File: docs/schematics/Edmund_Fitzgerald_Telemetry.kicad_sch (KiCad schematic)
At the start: 14 parts, among them Q1 MOSFET_N, Q2 MOSFET_N, U1 ESP32_Control, U2 MAX98357A, U3 DFPlayer_Pro, U4 ESP32-CAM

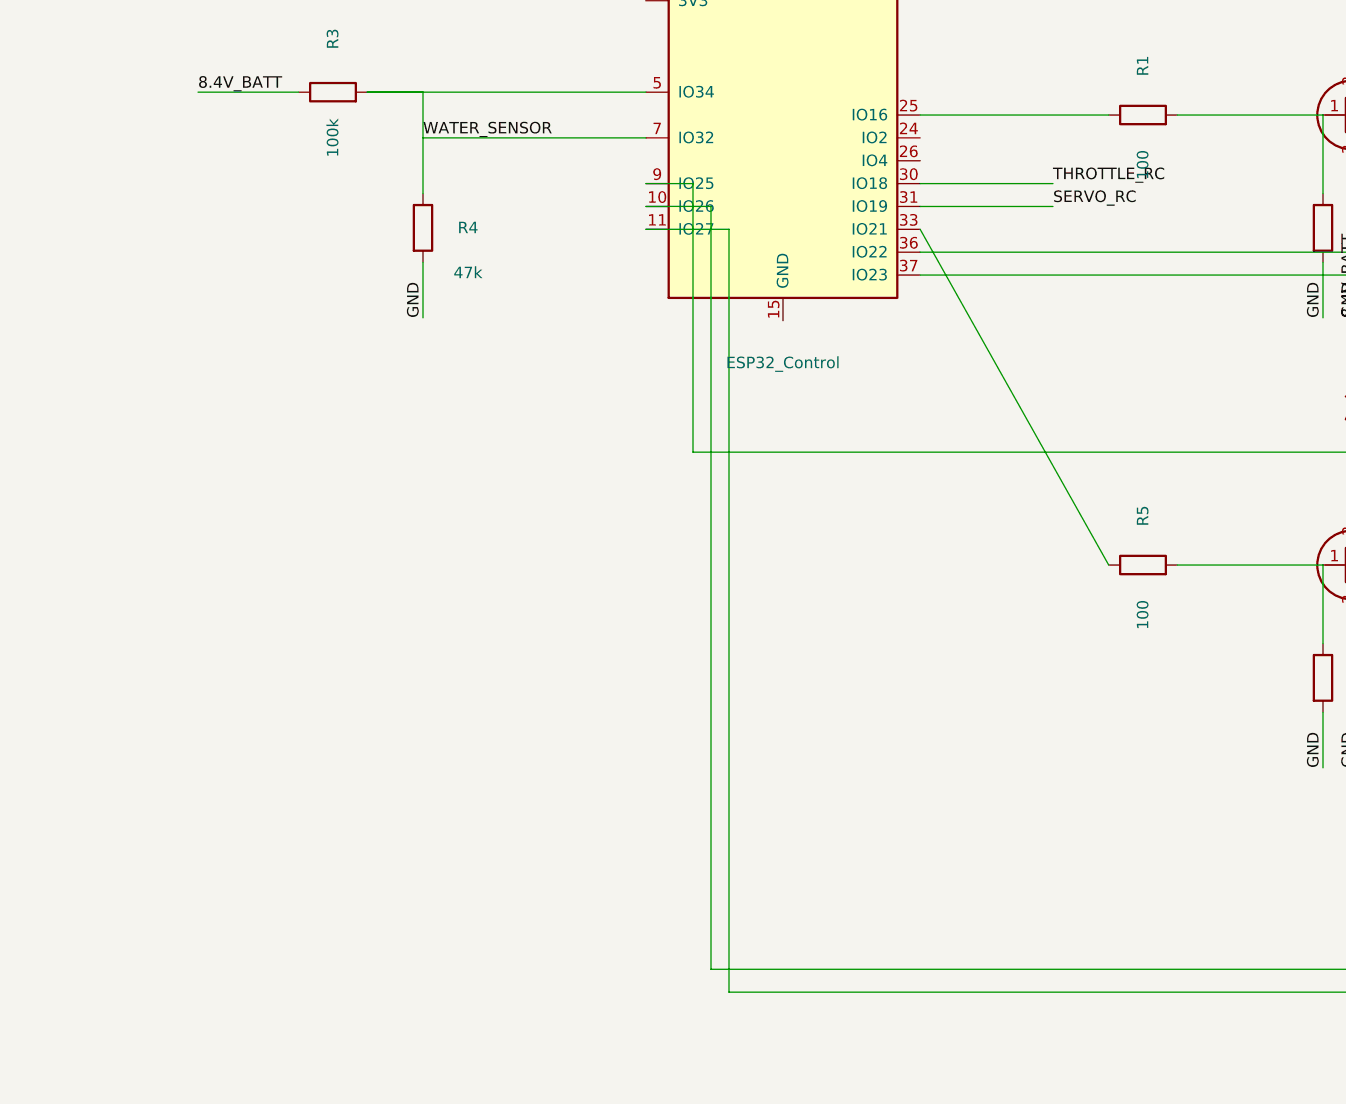
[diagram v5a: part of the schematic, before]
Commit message: Schematic update: Added physical RC and Servo wiring
- Replaced RC labels with physical orthogonal wires
- Connected RC Receiver (J1) and Rudder Servo (M1) to ESP32 pins
- Preserved all previous component work
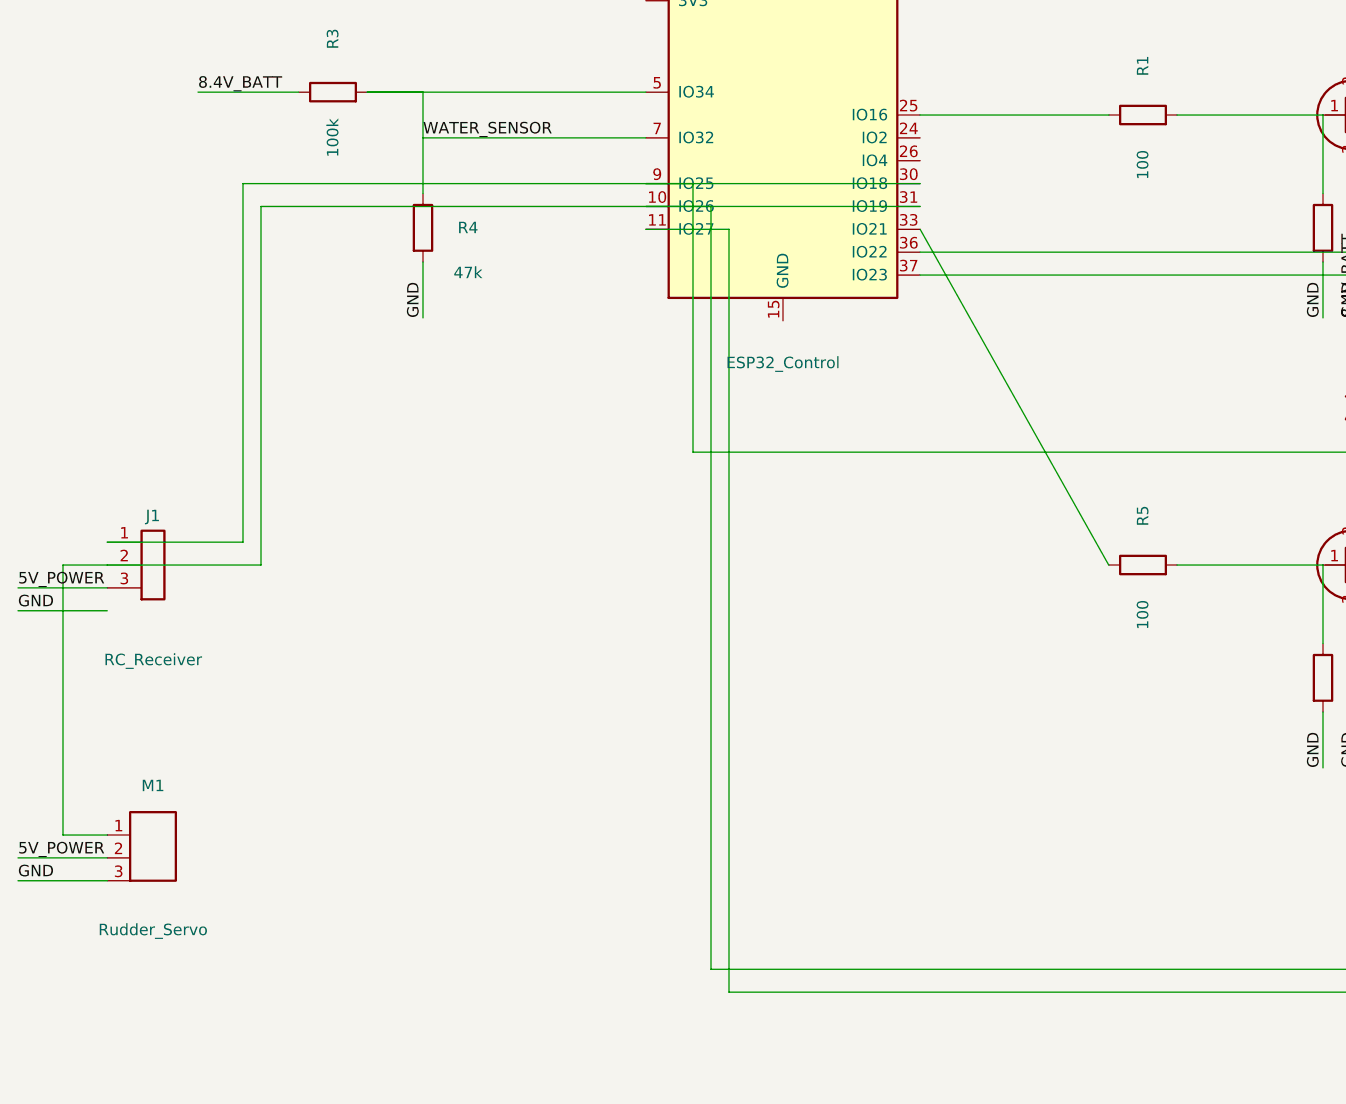
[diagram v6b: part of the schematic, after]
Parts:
- added J1: RC_Receiver, symbol Connector:Conn_01x03_Male
- added M1: Rudder_Servo, symbol Motor:Servo
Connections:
- net SERVO_RC is gone; now on an unnamed net: U1.31 (IO19)
- net THROTTLE_RC is gone; now on an unnamed net: U1.30 (IO18)
- net 5V_POWER: now also J1.3, M1.2 (VCC), M1.3 (GND)
- net at U1.10 (IO26), U3.3 (RX): now also J1.2, M1.1 (PWM)
- net at U1.9 (IO25), U2.3 (BCLK): now also J1.1
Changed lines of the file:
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@@
   (wire (pts (xy 247.3 189.84) (xy 240 189.84)) (stroke (width 0) (type solid)))
   (label "GND" (at 240 189.84 0) (effects (font (size 1.27 1.27)) (justify left bottom)))
-  (wire (pts (xy 165.24 105.08) (xy 180 105.08)) (stroke (width 0) (type solid)))
-  (label "THROTTLE_RC" (at 180 105.08 0) (effects (font (size 1.27 1.27)) (justify left bottom)))
-  (wire (pts (xy 165.24 107.62) (xy 180 107.62)) (stroke (width 0) (type solid)))
-  (label "SERVO_RC" (at 180 107.62 0) (effects (font (size 1.27 1.27)) (justify left bottom)))
+ (symbol (lib_id "Connector:Conn_01x03_Male") (at 80 150 0) (unit 1) (in_bom yes) (on_board yes) (property "Reference" "J1" (at 80 142 0)) (property "Value" "RC_Receiver" (at 80 158 0)))
+ (symbol (lib_id "Motor:Servo") (at 80 180 0) (unit 1) (in_bom yes) (on_board yes) (property "Reference" "M1" (at 80 172 0)) (property "Value" "Rudder_Servo" (at 80 188 0)))
+  (wire (pts (xy 74.92 144.92) (xy 90 144.92)) (stroke (width 0) (type solid)))
+  (wire (pts (xy 90 144.92) (xy 90 105.08)) (stroke (width 0) (type solid)))
+  (wire (pts (xy 90 105.08) (xy 165.24 105.08)) (stroke (width 0) (type solid)))
+  (wire (pts (xy 74.92 147.46) (xy 92 147.46)) (stroke (width 0) (type solid)))
+  (wire (pts (xy 92 147.46) (xy 92 107.62)) (stroke (width 0) (type solid)))
+  (wire (pts (xy 92 107.62) (xy 165.24 107.62)) (stroke (width 0) (type solid)))
+  (wire (pts (xy 74.92 147.46) (xy 70 147.46)) (stroke (width 0) (type solid)))
+  (wire (pts (xy 70 147.46) (xy 70 177.46)) (stroke (width 0) (type solid)))
+  (wire (pts (xy 70 177.46) (xy 74.92 177.46)) (stroke (width 0) (type solid)))
+  (wire (pts (xy 74.92 150) (xy 65 150)) (stroke (width 0) (type solid)))
+  (label "5V_POWER" (at 65 150 180) (effects (font (size 1.27 1.27)) (justify left bottom)))
+  (wire (pts (xy 74.92 152.54) (xy 65 152.54)) (stroke (width 0) (type solid)))
+  (label "GND" (at 65 152.54 180) (effects (font (size 1.27 1.27)) (justify left bottom)))
+  (wire (pts (xy 74.92 180) (xy 65 180)) (stroke (width 0) (type solid)))
+  (label "5V_POWER" (at 65 180 180) (effects (font (size 1.27 1.27)) (justify left bottom)))
+  (wire (pts (xy 74.92 182.54) (xy 65 182.54)) (stroke (width 0) (type solid)))
+  (label "GND" (at 65 182.54 180) (effects (font (size 1.27 1.27)) (justify left bottom)))
  (symbol (lib_id "Module:ESP32-CAM") (at 260 260 0) (unit 1) (in_bom yes) (on_board yes) (property "Reference" "U4" (at 260 245 0)) (property "Value" "ESP32-CAM" (at 260 275 0)))
   (wire (pts (xy 247.3 250) (xy 240 250)) (stroke (width 0) (type solid)))
@@
  (sheet_instances (path "/" (page "1")))
  (symbol_instances
-  (path "/6a6324be-f0d9-4660-bc5d-eeee538c9470" (reference "U1") (unit 1) (value "ESP32_Control") (footprint ""))
-  (path "/e6c6d49d-ded3-45c0-8657-80a2199d261a" (reference "Q1") (unit 1) (value "MOSFET_N") (footprint ""))
-  (path "/9c377b0d-e973-464f-ba9b-c0d3ee695c13" (reference "R1") (unit 1) (value "100") (footprint ""))
-  (path "/7128e088-a8e0-42b0-9125-83b782143666" (reference "R2") (unit 1) (value "10k") (footprint ""))
-  (path "/d0d04165-f706-4efb-a5ed-0caab7ad5f03" (reference "D1") (unit 1) (value "Running_Light") (footprint ""))
-  (path "/92d89f8a-660c-417e-aec4-9fac9af41bea" (reference "Q2") (unit 1) (value "MOSFET_N") (footprint ""))
-  (path "/e6ae053f-17f8-4cfd-a3d7-8c2b0e82cf8d" (reference "R5") (unit 1) (value "100") (footprint ""))
-  (path "/eb2263f6-fe29-44c1-9933-d479aa6b8725" (reference "R6") (unit 1) (value "10k") (footprint ""))
-  (path "/6b753ff5-9ad9-4527-975b-9cd45fada08d" (reference "D2") (unit 1) (value "Flood_Light") (footprint ""))
-  (path "/ee19817b-94e3-4076-bef5-0ab82a0e50dd" (reference "R3") (unit 1) (value "100k") (footprint ""))
-  (path "/9b2eb7d3-e64b-4f15-a07f-808149288232" (reference "R4") (unit 1) (value "47k") (footprint ""))
-  (path "/c80a82f1-7912-4ad3-b0df-f396f591f5cb" (reference "U2") (unit 1) (value "MAX98357A") (footprint ""))
-  (path "/81f42d43-b268-4c93-8496-6c3cabc9e4f4" (reference "U3") (unit 1) (value "DFPlayer_Pro") (footprint ""))
-  (path "/73432528-8c83-4b83-9f07-bf1c70c183ea" (reference "U4") (unit 1) (value "ESP32-CAM") (footprint ""))
+  (path "/59b94aab-b6f1-402e-a285-32c05f3e9cd8" (reference "U1") (unit 1) (value "ESP32_Control") (footprint ""))
+  (path "/18b471eb-c6e4-4014-9732-b24c33d6a4f0" (reference "Q1") (unit 1) (value "MOSFET_N") (footprint ""))
+  (path "/17f6d0a7-19d6-4950-b203-d8a34dd24ce9" (reference "R1") (unit 1) (value "100") (footprint ""))
+  (path "/426d630e-d918-489f-9237-ba41c97af636" (reference "R2") (unit 1) (value "10k") (footprint ""))
+  (path "/ba5084ae-150b-41df-8eb2-98f60ee789c5" (reference "D1") (unit 1) (value "Running_Light") (footprint ""))
+  (path "/e42cf439-7b2a-4e96-99f2-0b2adc51e860" (reference "Q2") (unit 1) (value "MOSFET_N") (footprint ""))
+  (path "/ccf70006-3938-4ee6-8397-a72c5893476f" (reference "R5") (unit 1) (value "100") (footprint ""))
+  (path "/919f3507-4d83-4838-b6e4-9a055e403494" (reference "R6") (unit 1) (value "10k") (footprint ""))
+  (path "/10b8eae2-e755-42b6-92ee-de969328f658" (reference "D2") (unit 1) (value "Flood_Light") (footprint ""))
+  (path "/f563a156-40d2-4f9d-9efa-69cbe097d550" (reference "R3") (unit 1) (value "100k") (footprint ""))
+  (path "/8e2f315a-81be-463c-9a7d-4e951deea1de" (reference "R4") (unit 1) (value "47k") (footprint ""))
+  (path "/2d758d59-8924-4800-8853-9ca61cb7b842" (reference "U2") (unit 1) (value "MAX98357A") (footprint ""))
+  (path "/8242a837-fcf7-4976-b44f-8c8d8ada560d" (reference "U3") (unit 1) (value "DFPlayer_Pro") (footprint ""))
+  (path "/388b7caa-1448-4ea5-8a13-c651ddf97cdf" (reference "J1") (unit 1) (value "RC_Receiver") (footprint ""))
+  (path "/97a4113d-5d86-4d30-aa3a-a567c6e848ae" (reference "M1") (unit 1) (value "Rudder_Servo") (footprint ""))
+  (path "/70cd39f3-6a68-450c-9ce3-bb51d21155a0" (reference "U4") (unit 1) (value "ESP32-CAM") (footprint ""))
  )
 )

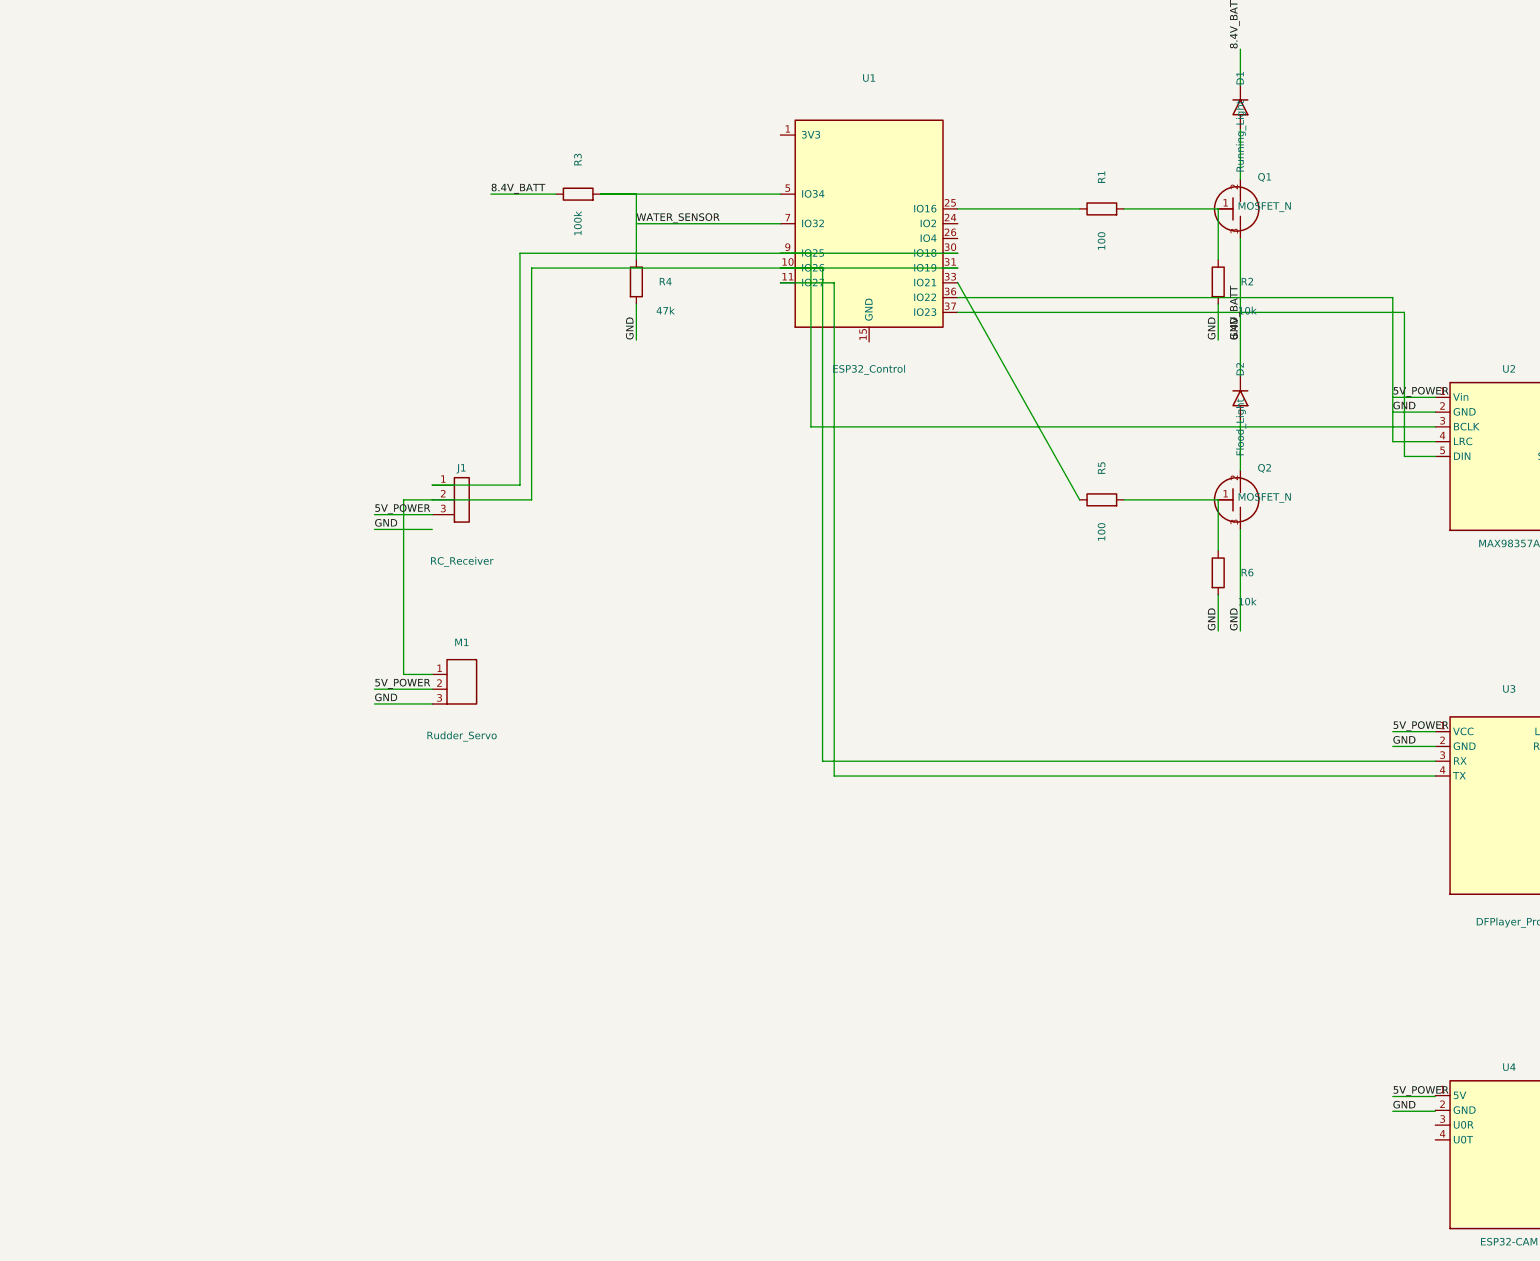
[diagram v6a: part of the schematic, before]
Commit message: Schematic v6.0: Full Physical Power & RC Integration
- Physical wiring from UBEC to ESP32 VIN/GND
- Physical power distribution to RC Receiver and Rudder Servo
- Updated ESP32 symbol to DevKit style with VIN pin
- All modules (Audio, Camera, Sensors, Lights) preserved and wired
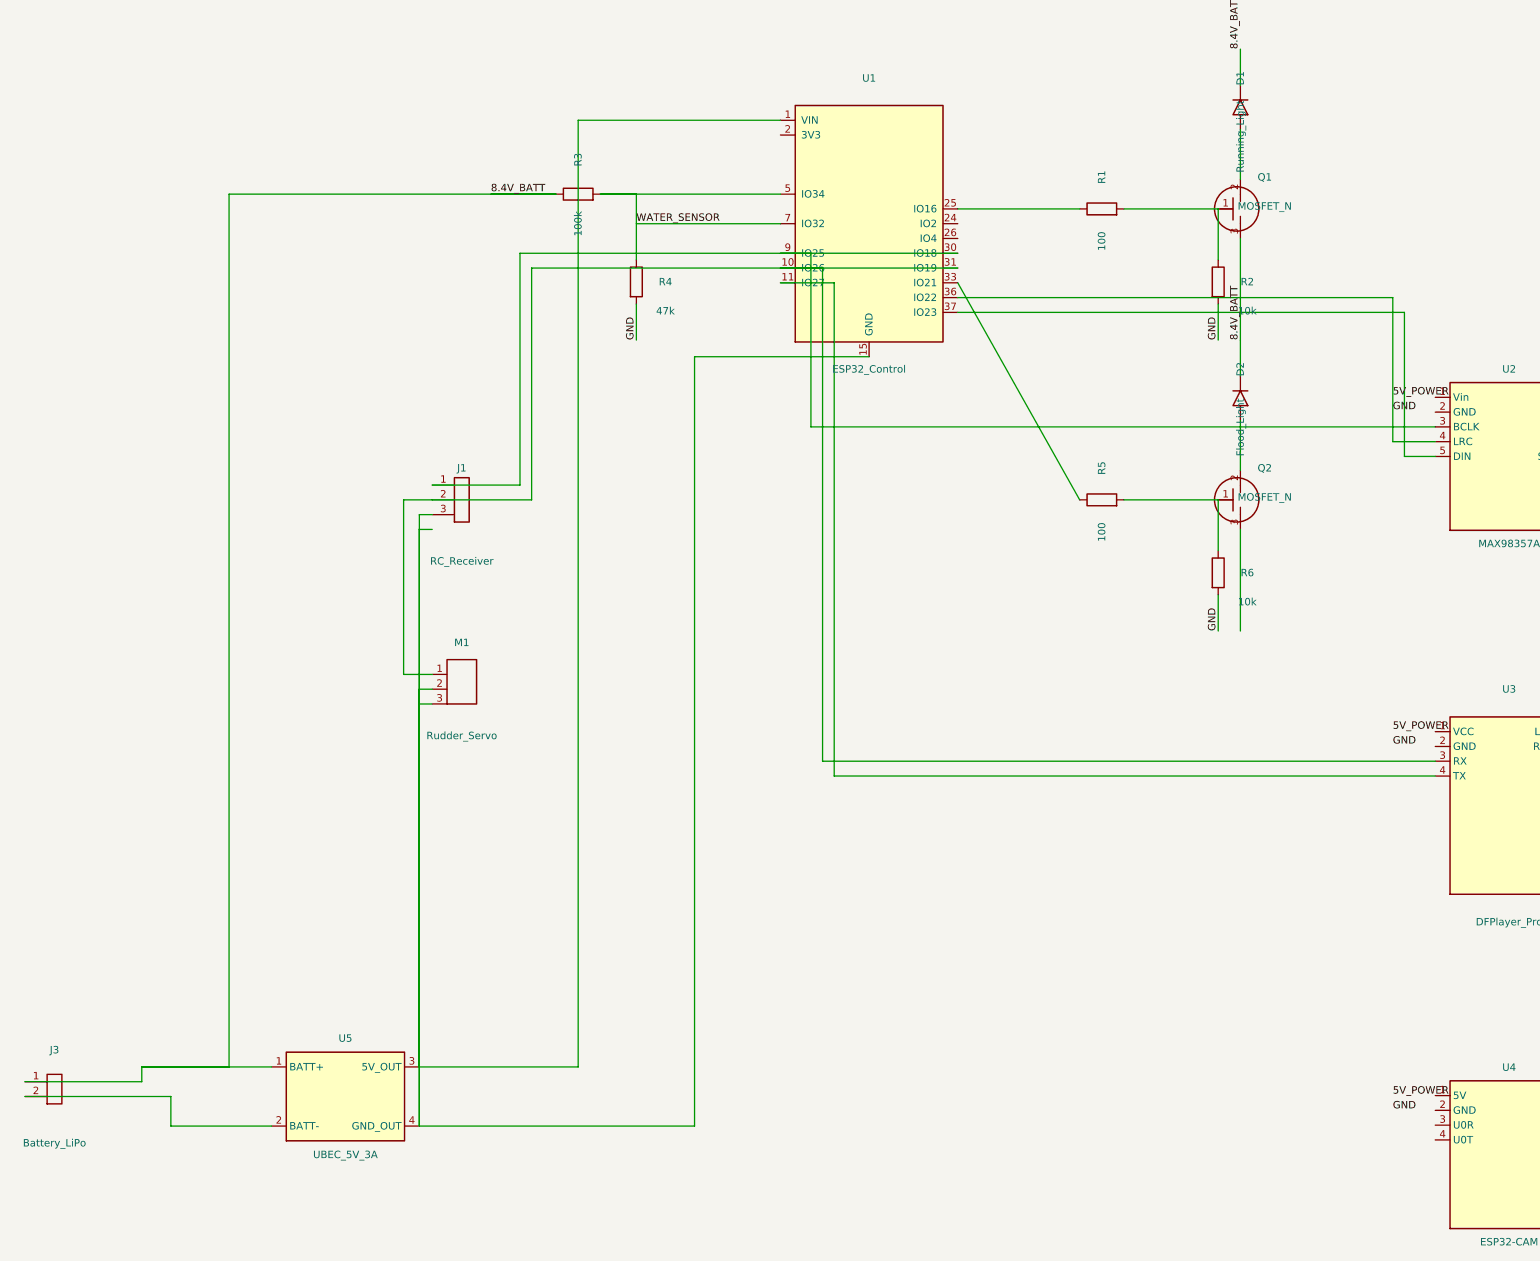
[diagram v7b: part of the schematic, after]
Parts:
- removed U1: ESP32_Control, symbol MCU_Espressif:ESP32-WROOM-32
- added J3: Battery_LiPo, symbol Connector:Conn_01x02_Male
- added U1: ESP32_Control, symbol MCU_Espressif:ESP32-DevKit
- added U5: UBEC_5V_3A, symbol Converter_DCDC:UBEC_5V
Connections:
- net 5V_POWER: now also U1.36 (IO22); no longer D1.2 (A), D2.2 (A), J1.3, M1.2 (VCC), M1.3 (GND), Q1.3 (S), Q2.3 (S), R3.1, U2.1 (Vin), U2.2 (GND), U3.1 (VCC), U3.2 (GND)
- net WATER_SENSOR: now also U1.5 (IO34), U1.7 (IO32)
- net at R1.1: now also U1.25 (IO16)
- net at J1.1, U2.3 (BCLK): now also U1.30 (IO18), U1.9 (IO25)
- net at U2.5 (DIN): now also U1.37 (IO23)
- net at J1.2, M1.1 (PWM), U3.3 (RX): now also U1.10 (IO26), U1.31 (IO19)
- net at U3.4 (TX): now also U1.11 (IO27)
- net at R5.1: now also U1.33 (IO21)
- new net: J1.3, M1.2 (VCC), M1.3 (GND), U1.1 (VIN), U1.15 (GND), U5.3 (5V_OUT), U5.4 (GND_OUT)
- new net: J3.2, U5.2 (BATT-)
- new net 8.4V_BATT: D1.2 (A), D2.2 (A), J3.1, Q1.3 (S), R3.1, U5.1 (BATT+)
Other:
- title: Edmund Fitzgerald - FULL SYSTEM -> Edmund Fitzgerald - MASTER SCHEMATIC
